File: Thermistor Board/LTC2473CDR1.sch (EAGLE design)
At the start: 31 parts, among them J1 282834-4, J2 I2C, J3 I2C in, J4 I2C out, U1 LTC2473IMS#PBF, U2 LTC2473IMS#PBF

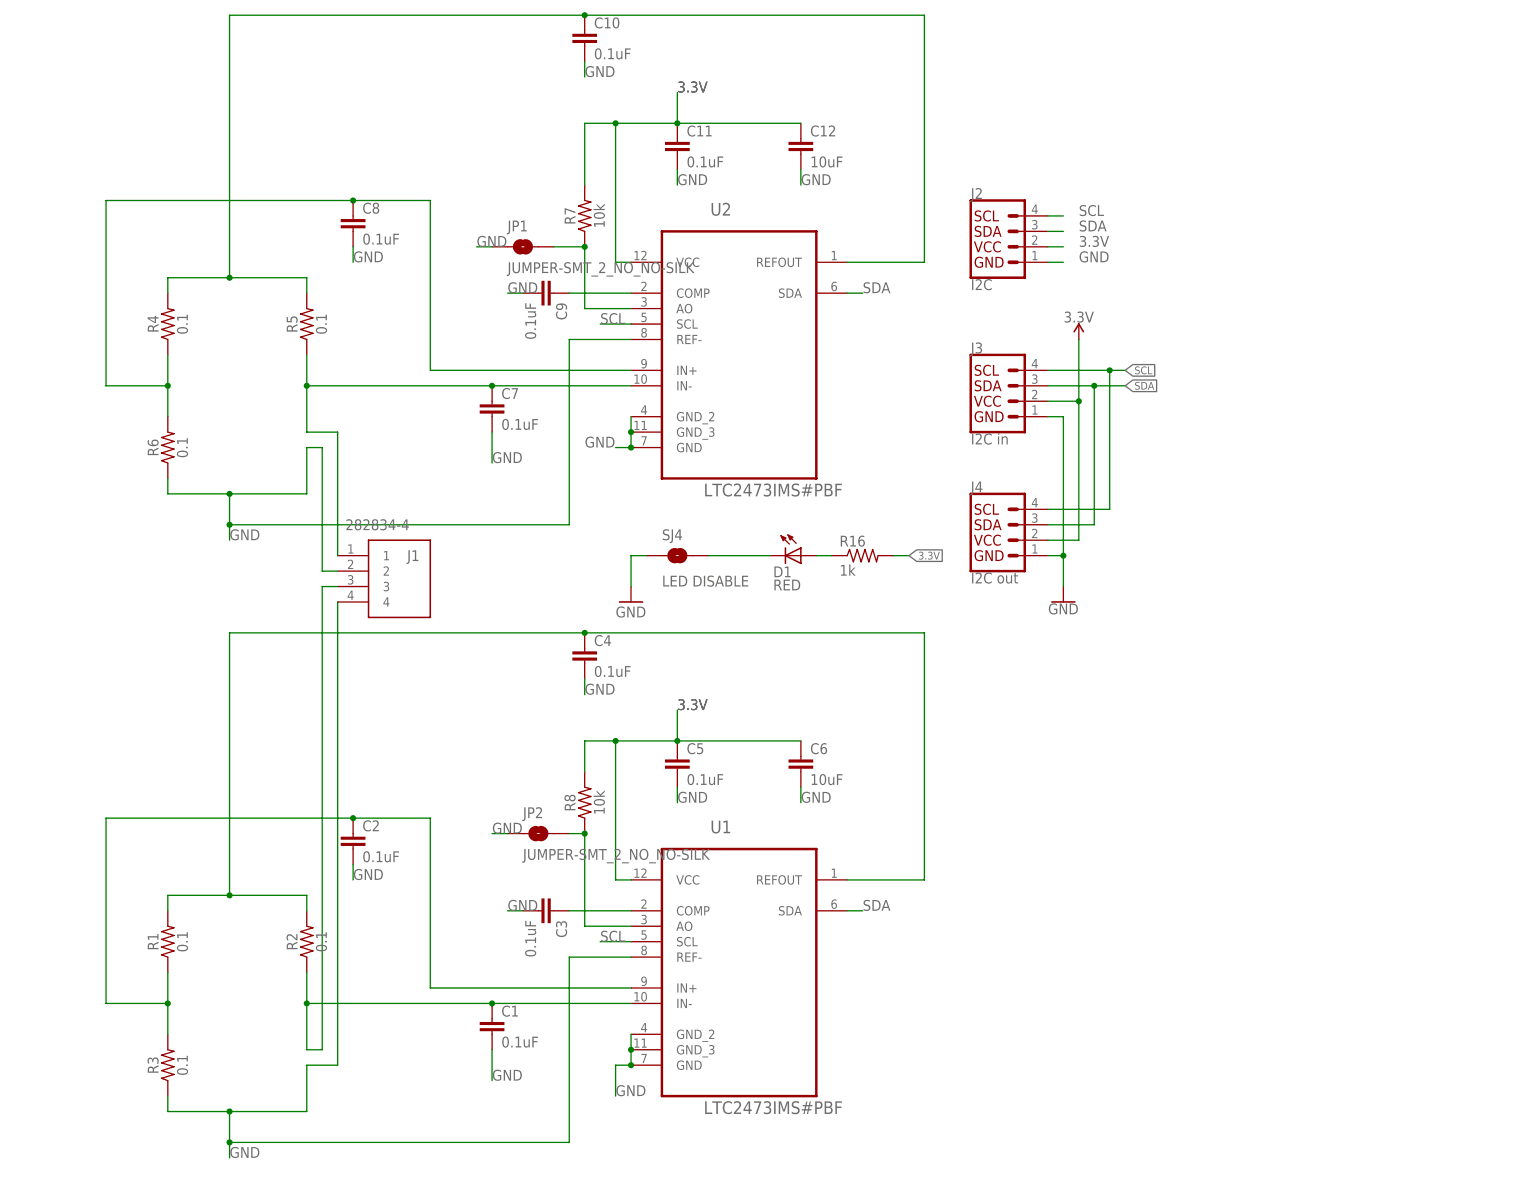
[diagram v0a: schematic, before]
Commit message: Thermistor Board
Thermistor board with BOM and GERBER files for manufacturing and assembly
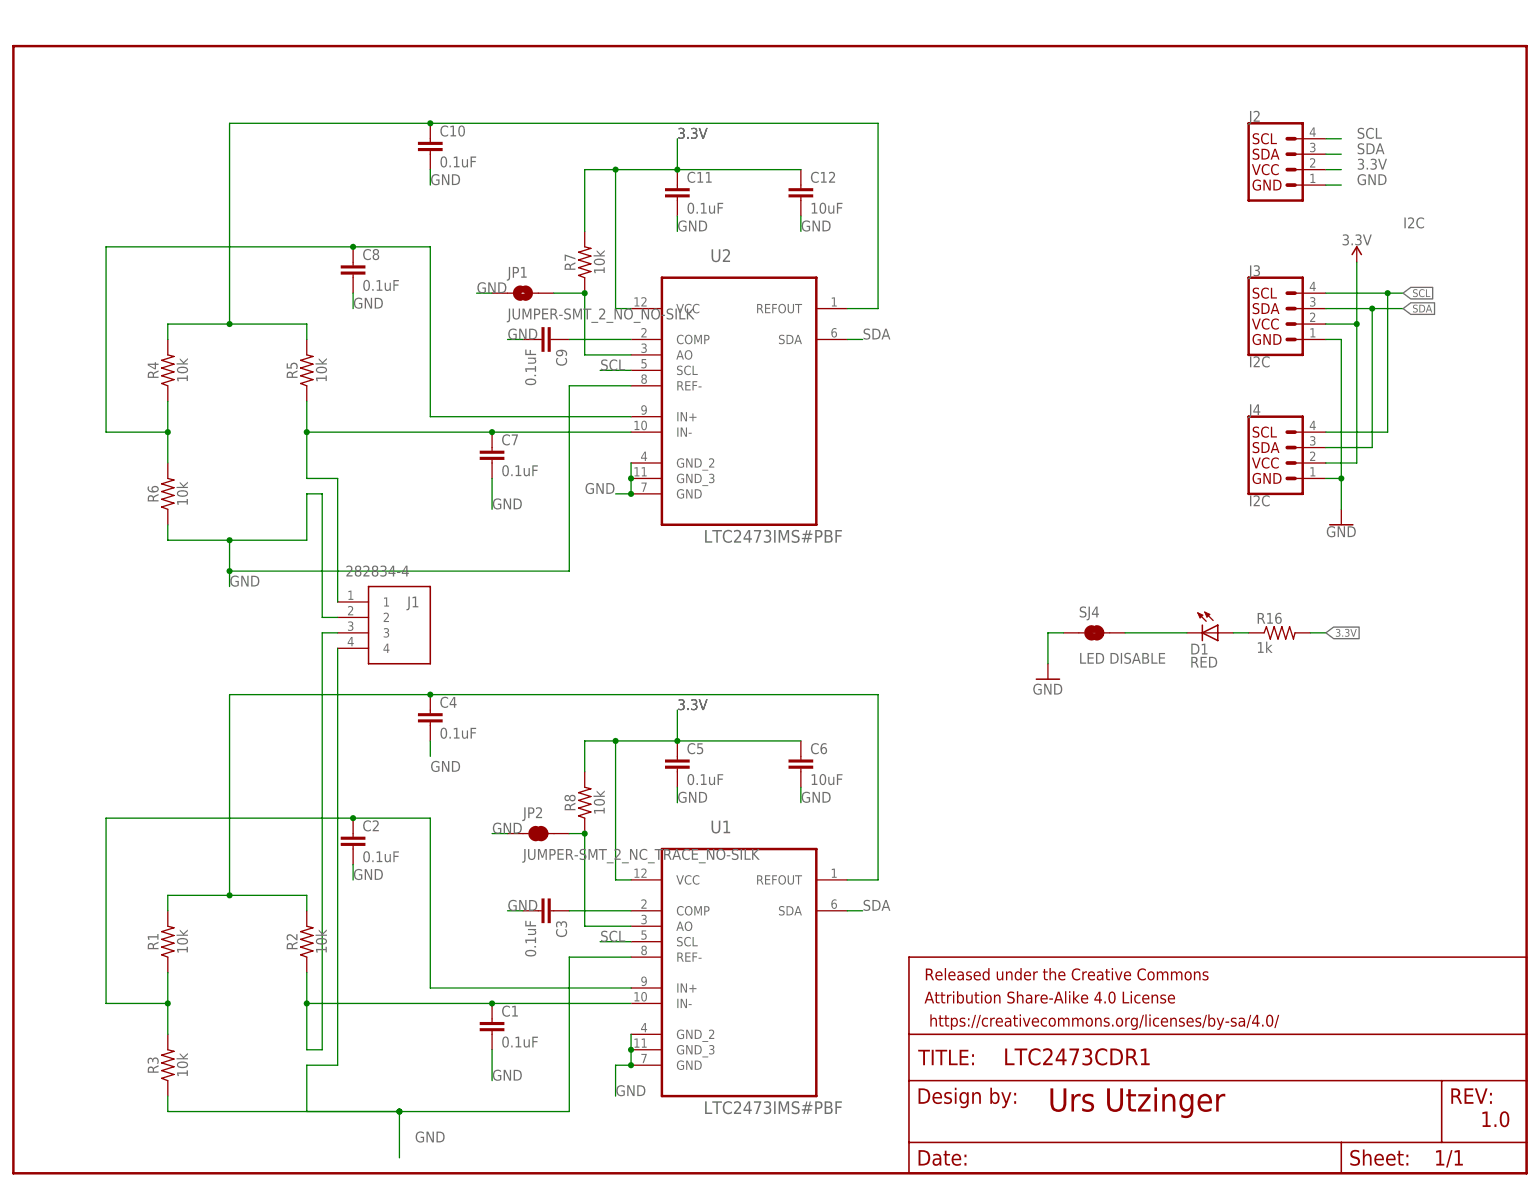
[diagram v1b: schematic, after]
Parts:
- added FRAME1: FRAME-LETTERNO_PACKAGE, SparkFun-Aesthetics:FRAME-LETTERNO_PACKAGE
- J3: value I2C in -> I2C
- J4: value I2C out -> I2C
- JP2: value JUMPER-SMT_2_NO_NO-SILK -> JUMPER-SMT_2_NC_TRACE_NO-SILK; device SparkFun-Jumpers:JUMPER-SMT_2_NO_NO-SILK -> SparkFun-Jumpers:JUMPER-SMT_2_NC_TRACE_NO-SILK
- R1, R2, R3, R4, R5, R6: value 0.1 -> 10k; device SparkFun-Resistors:0.1OHM-0603-1/3W-1% -> SparkFun-Resistors:10KOHM-0603-1/10W-1%
- R16: device SparkFun-Resistors:1K-1% -> SparkFun-Resistors:1KOHM-0603-1/10W-1%
- SJ4: device SparkFun-Passives:SOLDERJUMPERTRACE -> SparkFun-Jumpers:JUMPER-SMT_2_NC_TRACE_NO-SILK
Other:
- note added: "1.0"
- note added: "Urs Utzinger"
- moved on the sheet: C10, C11, C12, C4, C7, C8, C9, D1, J1, J2, J3, J4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
